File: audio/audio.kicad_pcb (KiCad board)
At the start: 2 copper layers, 52 x 52 mm, 62 parts, among them J1 Conn_01x02, J2 Conn_01x03, J3 Conn_01x05, U1 LM324DT, U2 LM324DT

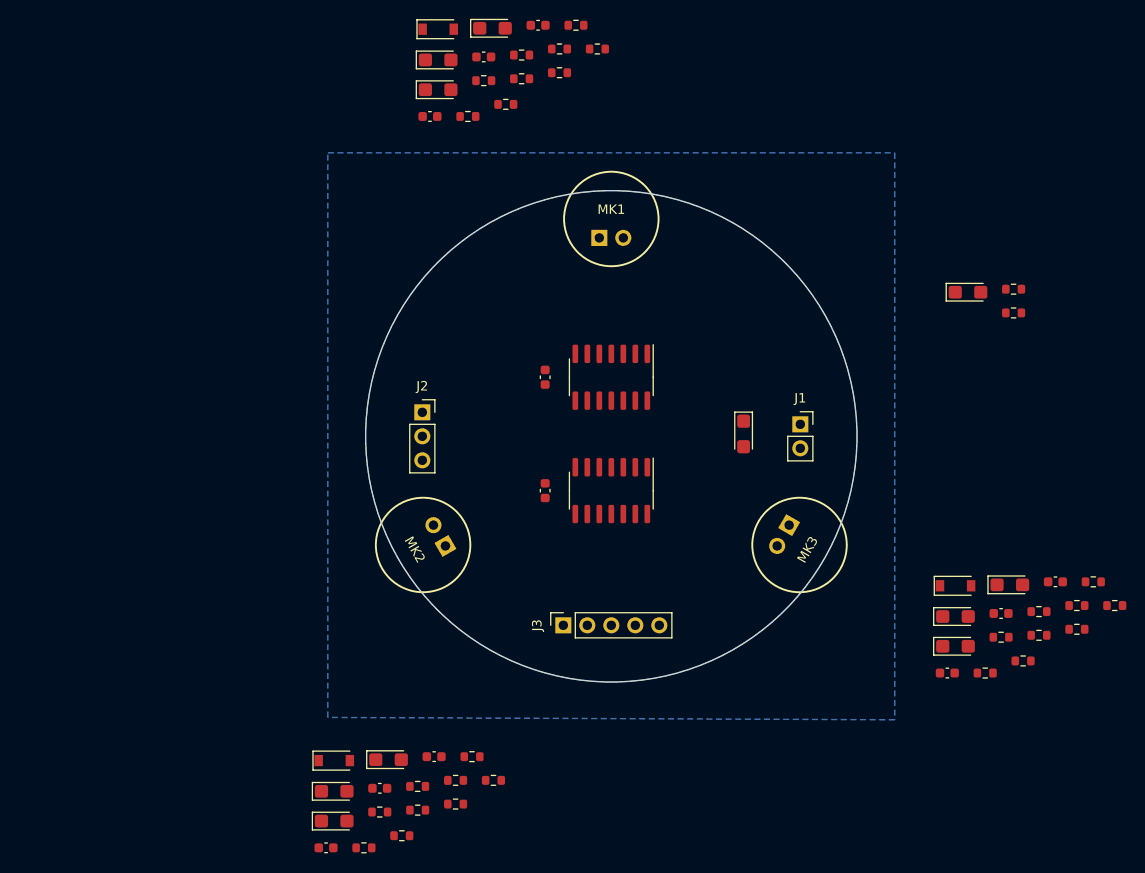
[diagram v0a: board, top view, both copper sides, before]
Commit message: properly orient pcb
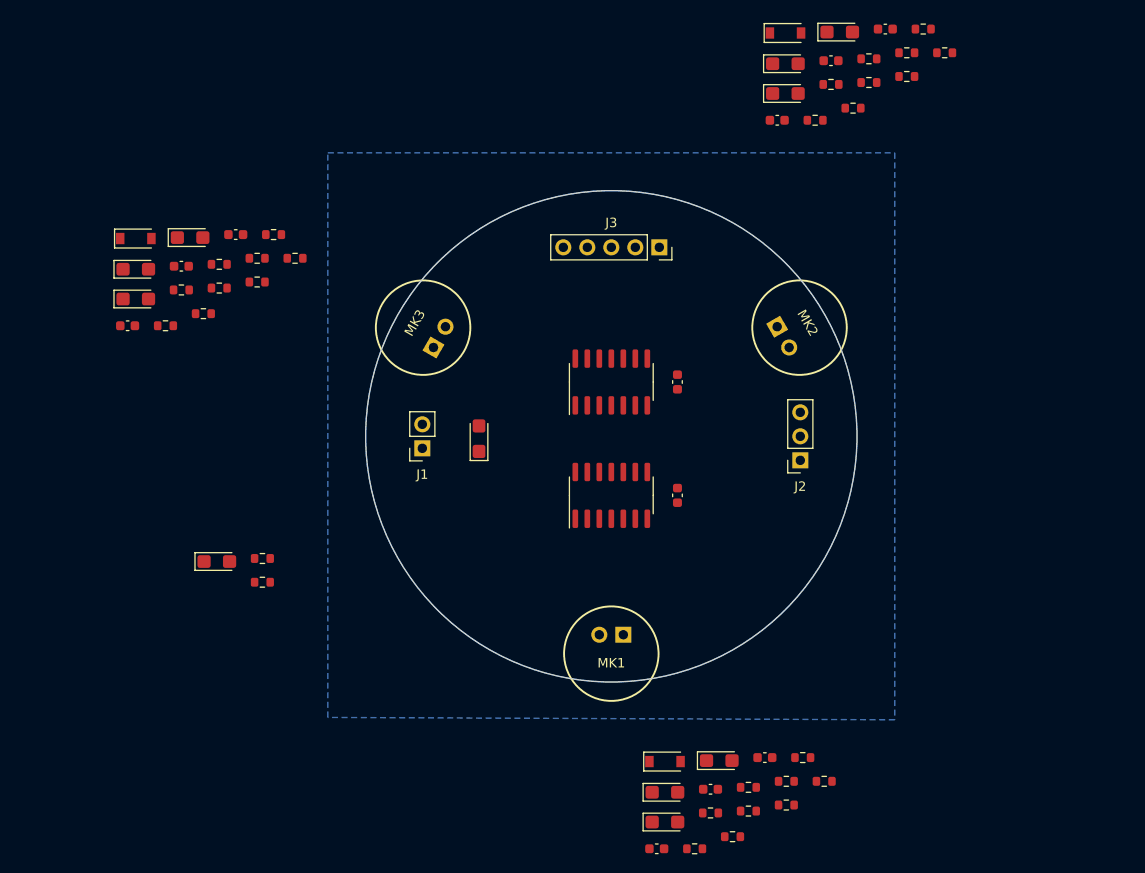
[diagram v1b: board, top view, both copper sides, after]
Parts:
- moved R22 94.2 mm to (108.9, 78.3)
- moved R24 94.2 mm to (114.6, 75.2)
- moved R25 94.2 mm to (108.9, 80.9)
- moved C17 94.2 mm to (104.8, 78.5)
- moved C18 94.2 mm to (110.6, 75.2)
- moved C19 94.2 mm to (100.0, 78.9)
- moved C20 94.2 mm to (99.2, 84.8)
- moved C21 94.2 mm to (105.8, 75.5)
- moved C22 94.2 mm to (100.0, 82.0)
- moved D3 94.2 mm to (100.0, 75.6)
- moved R21 94.2 mm to (104.8, 81.1)
- moved R26 94.2 mm to (112.9, 77.7)
- moved R27 94.2 mm to (107.2, 83.6)
- moved R28 94.2 mm to (112.9, 80.2)
- moved R29 94.2 mm to (116.9, 77.7)
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
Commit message: kind of messed with the "rats nest"
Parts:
- moved R8 38.7 mm to (161.8, 95.0)
- moved R3 37.9 mm to (161.8, 98.5), turned to 180 degrees
- moved C8 37.5 mm to (157.1, 102.8), turned to 180 degrees
- moved C5 37.1 mm to (161.8, 96.8), turned to 180 degrees
- moved R7 34.7 mm to (163.5, 101.5), turned to 180 degrees
- moved C10 34.5 mm to (168.2, 105.0)
- moved R11 34.0 mm to (173.8, 99.0)
- moved R9 33.9 mm to (162.0, 105.0)
- moved R5 33.1 mm to (153.6, 107.5), turned to 180 degrees
- moved R10 33.0 mm to (162.0, 103.3)
- moved C9 32.8 mm to (165.8, 98.3), turned to 180 degrees
- moved C6 31.0 mm to (157.1, 101.0), turned to 180 degrees
- moved D1 30.9 mm to (168.1, 102.5), turned to 180 degrees
- moved R6 30.5 mm to (166.6, 100.3)
- moved C7 26.7 mm to (149.8, 108.3)
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
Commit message: routing wires
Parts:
- moved C3 33.5 mm to (142.0, 107.0)
- moved R2 28.9 mm to (141.4, 105.0)
- moved R1 28.8 mm to (141.5, 103.2), turned to 180 degrees
- moved C5 21.2 mm to (146.8, 111.8)
- moved C1 19.7 mm to (144.8, 102.5)
- moved R3 19.0 mm to (146.8, 110.0)
- moved R6 14.2 mm to (161.5, 113.5)
- moved R11 12.4 mm to (164.8, 107.5), turned to 180 degrees
- moved D1 11.5 mm to (160.6, 111.3)
- moved R4 11.5 mm to (151.1, 110.0)
- moved R8 7.61 mm to (157.1, 101.0)
- moved C9 6.56 mm to (160.8, 102.5), turned to 270 degrees
- moved R7 5.51 mm to (160.3, 106.0)
- moved R10 4.52 mm to (161.6, 107.8), turned to 180 degrees
- moved R9 4.43 mm to (159.1, 108.4), turned to 270 degrees
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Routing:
- net +5V: track 0.00 -> 71.0 mm
- net Net-(C5-Pad2): track 0.00 -> 64.1 mm
- net +2V5: track 0.00 -> 43.1 mm
- net GND: track 0.00 -> 39.1 mm, vias 0 -> 2
- net A0: track 0.00 -> 18.3 mm
- net Net-(C10-Pad1): track 0.00 -> 16.6 mm
- net Net-(C7-Pad2): track 0.00 -> 10.3 mm
- net Net-(C8-Pad2): track 0.00 -> 8.16 mm
- net Net-(C5-Pad1): track 0.00 -> 6.62 mm
- net Net-(C6-Pad1): track 0.00 -> 5.76 mm
- net Net-(C9-Pad2): track 0.00 -> 4.55 mm
- net Net-(C9-Pad1): track 0.00 -> 2.99 mm

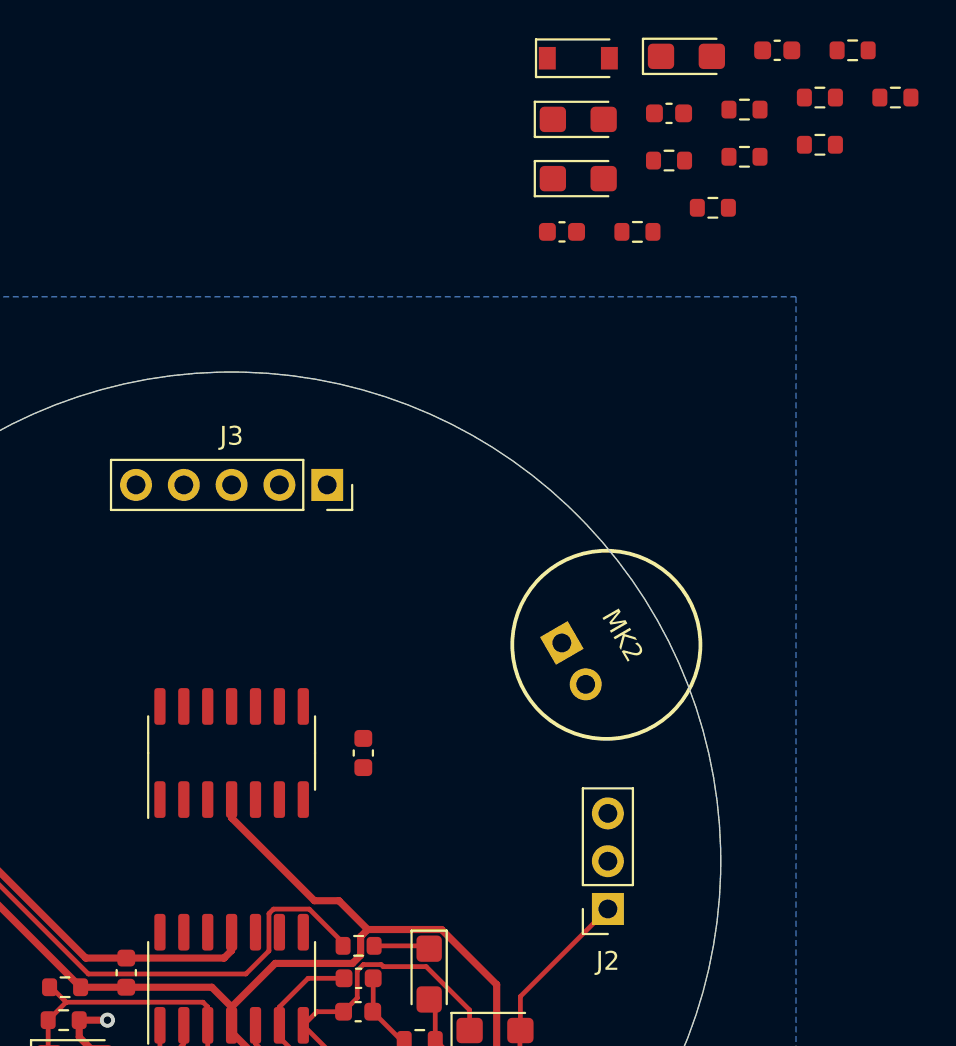
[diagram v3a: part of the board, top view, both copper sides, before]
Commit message: 2nd mic added
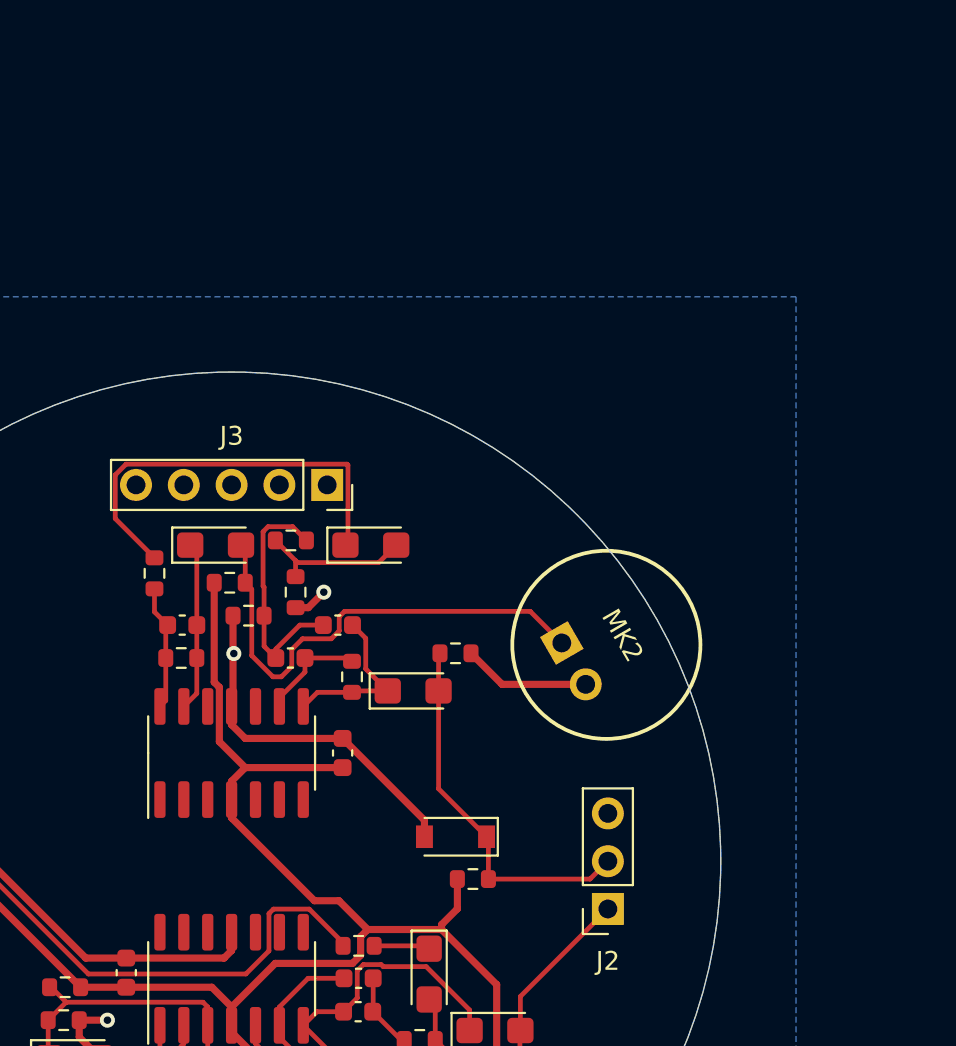
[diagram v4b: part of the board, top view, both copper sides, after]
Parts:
- moved R15 48.5 mm to (163.2, 97.5)
- moved R17 43.5 mm to (146.2, 81.2), turned to 90 degrees
- moved D2 41.9 mm to (162.2, 95.2), turned to 180 degrees
- moved C12 38.5 mm to (156.0, 84.0)
- moved R20 37.7 mm to (162.2, 85.5)
- moved C11 37.5 mm to (147.7, 84.0), turned to 180 degrees
- moved R13 37.2 mm to (150.2, 81.8)
- moved R12 37.0 mm to (147.7, 85.8), turned to 180 degrees
- moved R19 36.6 mm to (153.8, 82.2), turned to 270 degrees
- moved R18 32.9 mm to (151.2, 83.5), turned to 180 degrees
- moved R16 31.6 mm to (153.5, 79.5)
- moved C15 30.9 mm to (157.8, 79.8)
- moved C13 29.7 mm to (149.5, 79.8)
- moved C16 28.6 mm to (160.0, 87.5)
- moved R14 28.1 mm to (156.8, 86.8), turned to 90 degrees
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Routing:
- net GND: track 39.1 -> 66.8 mm, vias 2 -> 4
- net Net-(C13-Pad2): track 0.00 -> 26.2 mm
- net Net-(C15-Pad1): track 0.00 -> 22.2 mm
- net +5V: track 71.0 -> 91.7 mm
- net A1: track 0.00 -> 19.9 mm
- net Net-(C12-Pad1): track 0.00 -> 13.2 mm
- net Net-(C12-Pad2): track 0.00 -> 9.11 mm
- net Net-(C11-Pad1): track 0.00 -> 9.01 mm
- net Net-(C15-Pad2): track 0.00 -> 8.15 mm
- net Net-(C11-Pad2): track 0.00 -> 6.71 mm
- net Net-(C14-Pad2): track 0.00 -> 5.71 mm

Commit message: fix design rules
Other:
- rule trace_min: 0.2 -> 0.127
- rule via_min_size: 0.4 -> 0.6
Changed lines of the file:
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@@
-(kicad_pcb (version 20171130) (host pcbnew "(5.1.9)-1")
+(kicad_pcb (version 20171130) (host pcbnew "(5.1.8)-1")
   (general
     (thickness 1.6)
@@
     (zone_clearance 0.508)
     (zone_45_only no)
-    (trace_min 0.2)
+    (trace_min 0.127)
     (via_size 0.6)
     (via_drill 0.3)
-    (via_min_size 0.4)
+    (via_min_size 0.6)
     (via_min_drill 0.3)
     (uvia_size 0.6)
     (uvia_drill 0.3)
     (uvias_allowed no)
-    (uvia_min_size 0.2)
-    (uvia_min_drill 0.1)
+    (uvia_min_size 0.6)
+    (uvia_min_drill 0.3)
     (edge_width 0.05)
     (segment_width 0.2)
@@
     (solder_mask_min_width 0.264)
     (aux_axis_origin 0 0)
+    (grid_origin 150.35 96.55)
     (visible_elements 7FFFFFFF)
     (pcbplotparams
@@
       (effects (font (size 1 1) (thickness 0.15)))
     )
-    (fp_text user %R (at 0 0) (layer F.Fab)
-      (effects (font (size 0.4 0.4) (thickness 0.06)))
-    )
     (fp_line (start -0.8 0.4) (end -0.8 -0.4) (layer F.Fab) (width 0.1))
     (fp_line (start -0.8 -0.4) (end 0.8 -0.4) (layer F.Fab) (width 0.1))
@@
     (fp_line (start 1.48 -0.73) (end 1.48 0.73) (layer F.CrtYd) (width 0.05))
     (fp_line (start 1.48 0.73) (end -1.48 0.73) (layer F.CrtYd) (width 0.05))
+    (fp_text user %R (at 0 0) (layer F.Fab)
+      (effects (font (size 0.4 0.4) (thickness 0.06)))
+    )
     (pad 1 smd roundrect (at -0.775 0) (size 0.9 0.95) (layers F.Cu F.Paste F.Mask) (roundrect_rratio 0.25)
       (net 30 "Net-(C12-Pad1)"))

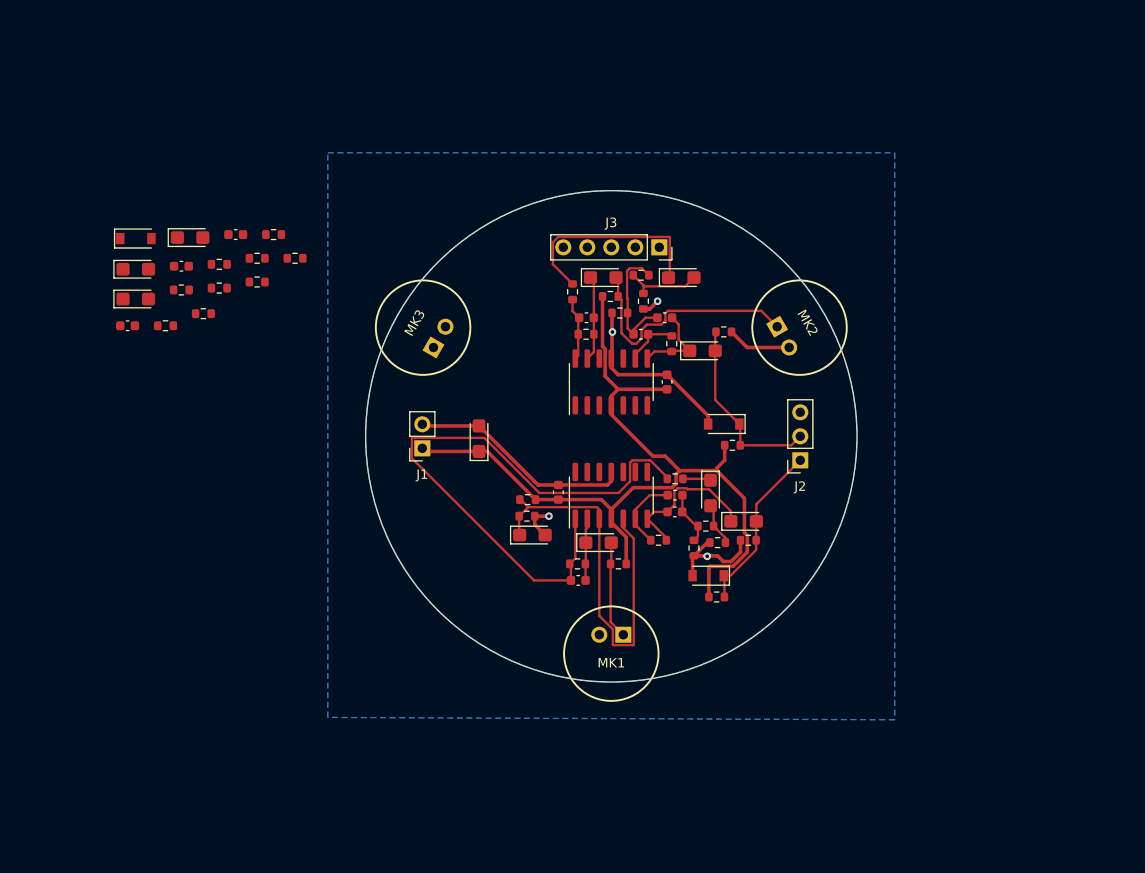
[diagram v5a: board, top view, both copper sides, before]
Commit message: resize boards
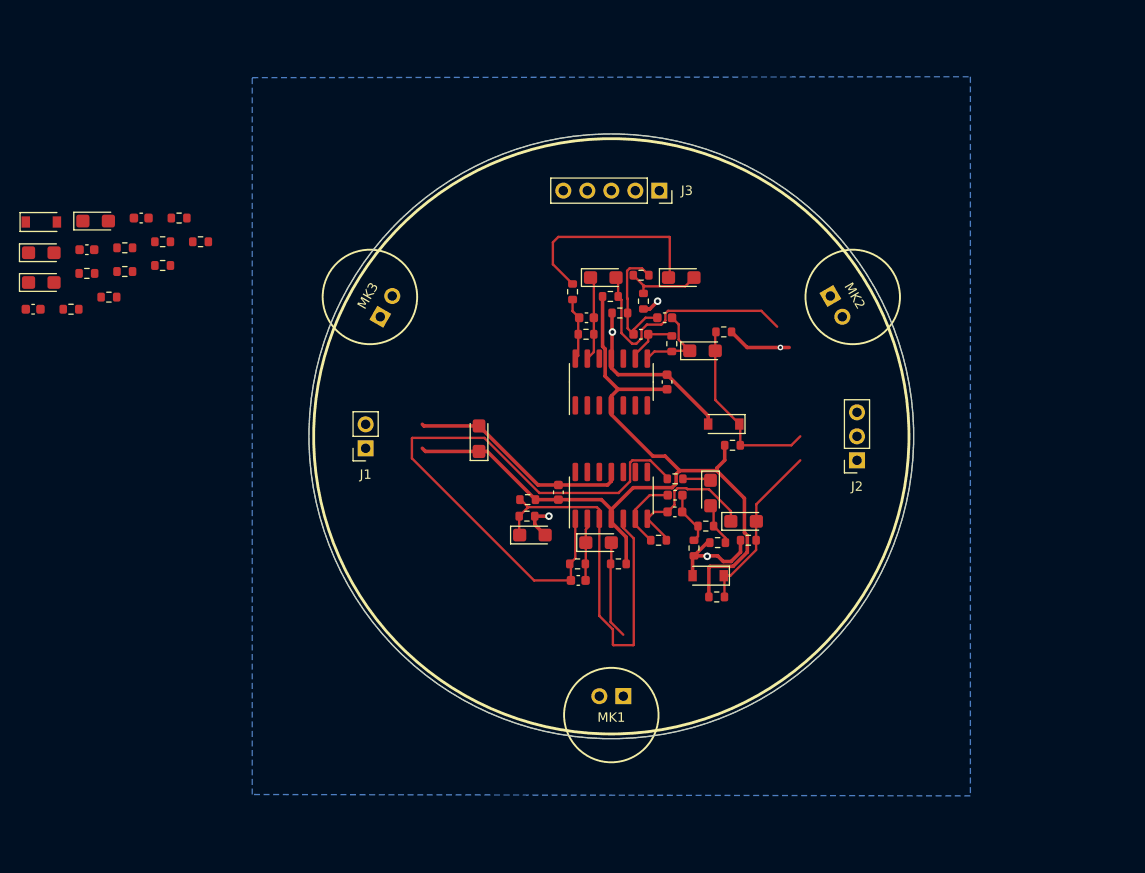
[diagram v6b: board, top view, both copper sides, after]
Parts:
- moved C17 10.2 mm to (94.8, 76.8)
- moved C18 10.2 mm to (100.6, 73.5)
- moved C19 10.2 mm to (90.0, 77.1)
- moved C20 10.2 mm to (89.2, 83.1)
- moved C21 10.2 mm to (95.8, 73.8)
- moved C22 10.2 mm to (90.0, 80.3)
- moved D3 10.2 mm to (90.0, 73.9)
- moved R21 10.2 mm to (94.8, 79.3)
- moved R22 10.2 mm to (98.9, 76.6)
- moved R23 10.2 mm to (93.2, 83.1)
- moved R24 10.2 mm to (104.6, 73.5)
- moved R25 10.2 mm to (98.9, 79.1)
- moved R26 10.2 mm to (102.9, 76.0)
- moved R27 10.2 mm to (97.2, 81.8)
- moved R28 10.2 mm to (102.9, 78.5)
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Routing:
- net GND: vias 4 -> 5
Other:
- board size 52 x 52 mm -> 64 x 64 mm

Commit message: Finished adding audio pcb tracks
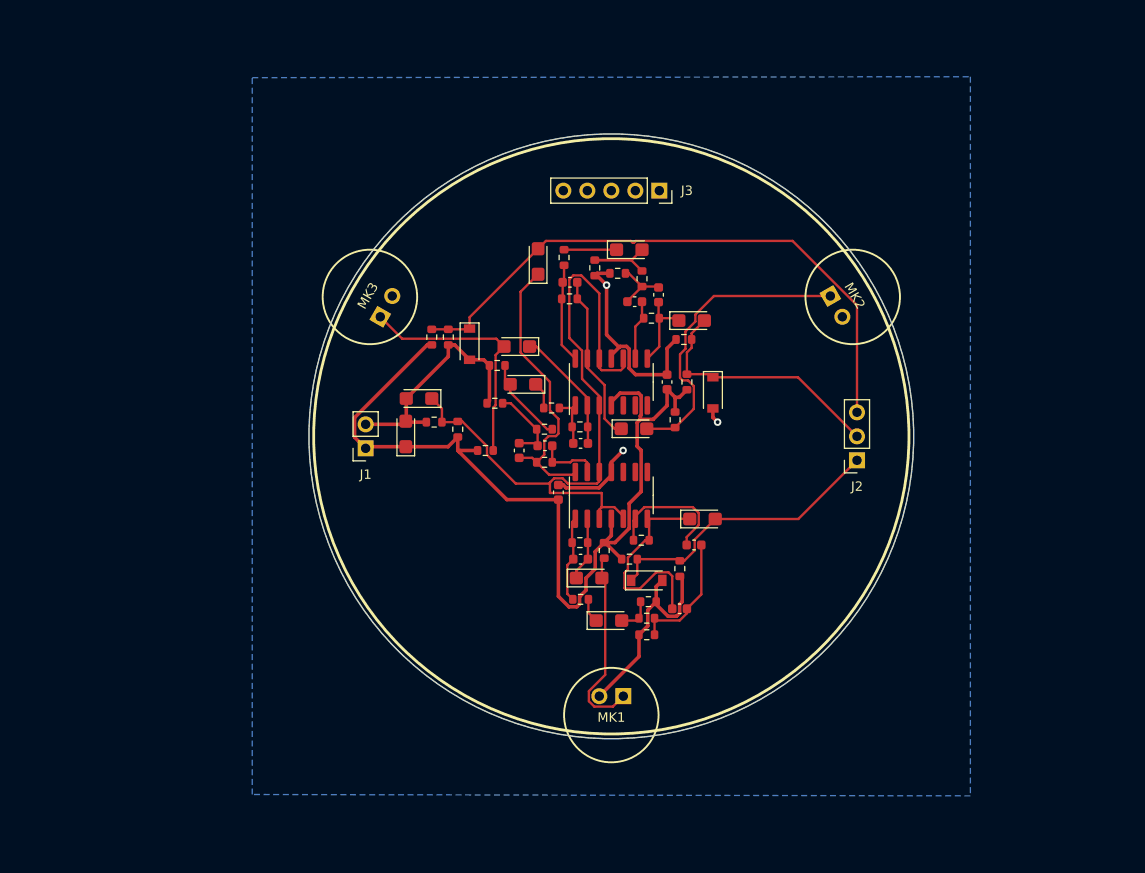
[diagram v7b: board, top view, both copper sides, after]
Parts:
- moved C17 56.1 mm to (147.1, 97.3), turned to 180 degrees
- moved C20 56.1 mm to (143.3, 97.5)
- moved R21 54.6 mm to (147.0, 95.5), turned to 180 degrees
- moved R23 52.7 mm to (143.3, 99.3)
- moved C22 52.6 mm to (142.6, 78.0), turned to 90 degrees
- moved C19 51.3 mm to (140.3, 87.0), turned to 180 degrees
- moved C21 48.4 mm to (141.0, 91.0), turned to 180 degrees
- moved R25 47.4 mm to (143.3, 95.8), turned to 180 degrees
- moved D3 47.1 mm to (135.3, 86.8), turned to 270 degrees
- moved C18 47.0 mm to (140.6, 98.0), turned to 270 degrees
- moved R26 44.8 mm to (144.0, 93.5), turned to 180 degrees
- moved R22 43.8 mm to (137.0, 98.0)
- moved R27 42.4 mm to (138.0, 93.0), turned to 180 degrees
- moved R28 37.0 mm to (138.3, 89.0), turned to 180 degrees
- moved R24 29.6 mm to (131.3, 86.0), turned to 90 degrees
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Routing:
- net A2: track 0.00 -> 63.9 mm
- net Net-(C5-Pad2): track 64.1 -> 9.22 mm
- net +2V5: track 43.1 -> 74.2 mm
- net Net-(C18-Pad2): track 0.00 -> 30.5 mm
- net Net-(C19-Pad2): track 0.00 -> 25.9 mm
- net Net-(C15-Pad1): track 22.2 -> 5.55 mm
- net GND: track 66.8 -> 83.2 mm, vias 5 -> 3
- net Net-(C17-Pad1): track 0.00 -> 13.2 mm
- net A0: track 18.3 -> 30.9 mm
- net Net-(C7-Pad2): track 10.3 -> 20.4 mm
- net Net-(C21-Pad2): track 0.00 -> 9.13 mm
- net Net-(C11-Pad1): track 9.01 -> 17.8 mm
- net Net-(C18-Pad1): track 0.00 -> 8.59 mm
- net Net-(C6-Pad1): track 5.76 -> 13.4 mm
- net +5V: track 91.7 -> 99.3 mm
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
